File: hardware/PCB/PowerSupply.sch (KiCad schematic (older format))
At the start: 15 parts, among them IC1 BQ24092DGQR, IC4 TPS62291DRVR, J3 S2B-XH-A_LF__SN_

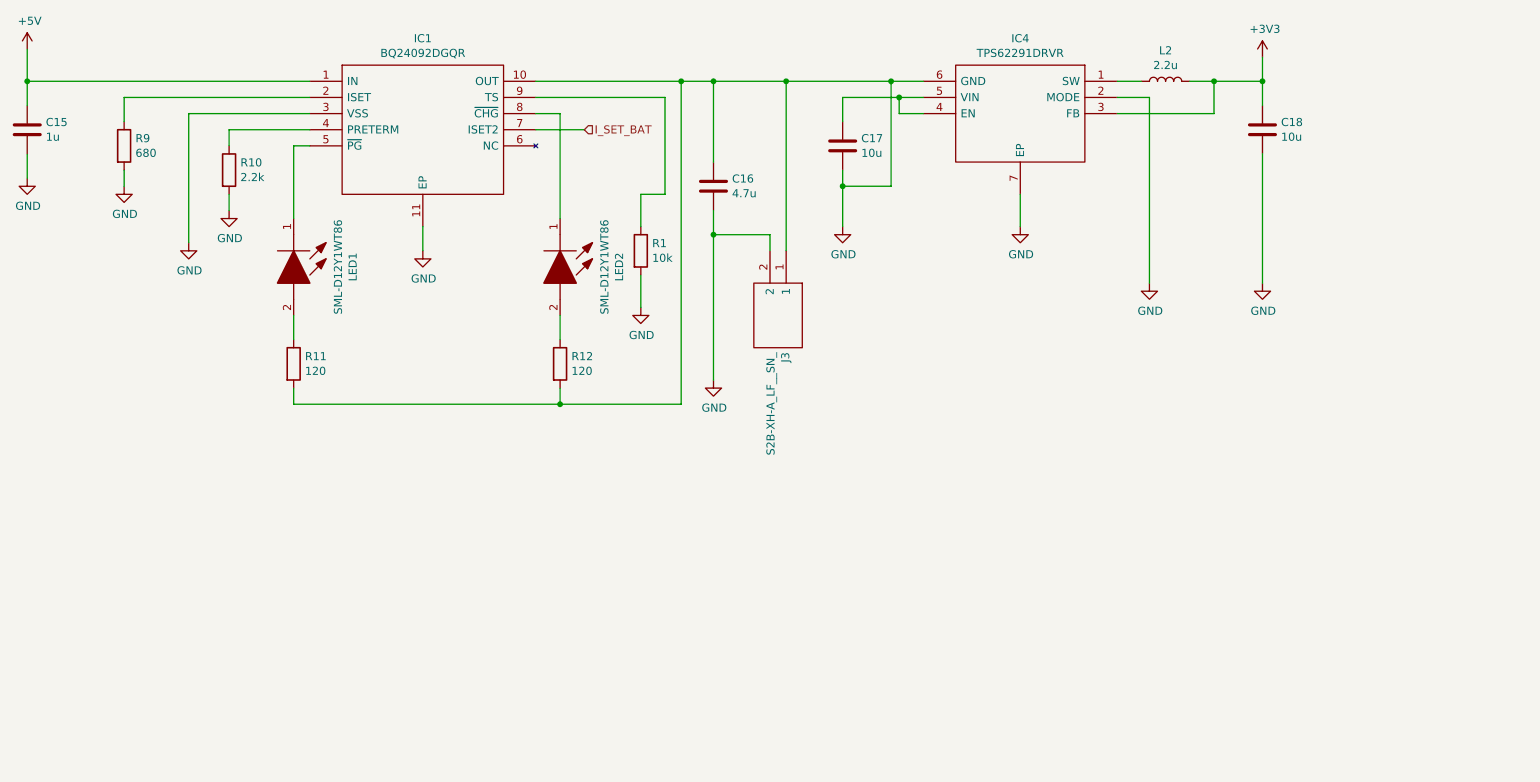
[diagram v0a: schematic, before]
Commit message: add inductor footprint LPS4018
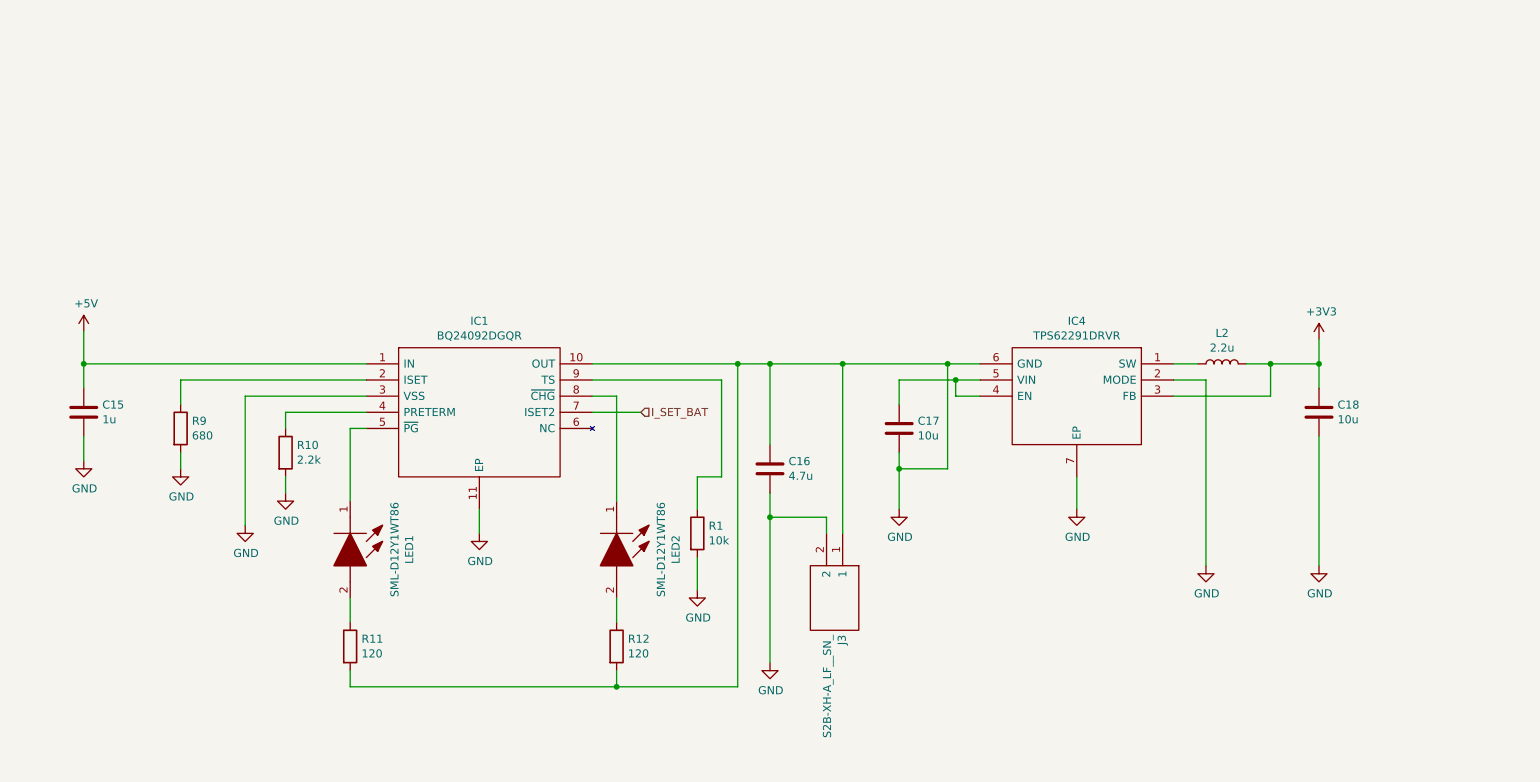
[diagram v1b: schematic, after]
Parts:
- C18: footprint (none) -> Capacitor_SMD:C_0603_1608Metric
- L2: footprint (none) -> Inductor_SMD:L_Coilcraft_LPS4018; Mouser Part Number (none) -> 994-LPS4018-222MRB
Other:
- moved on the sheet: C15, C16, C17, C18, IC1, IC4, J3, L2, LED1, LED2, R1, R10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

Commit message: corrected power supply schematic
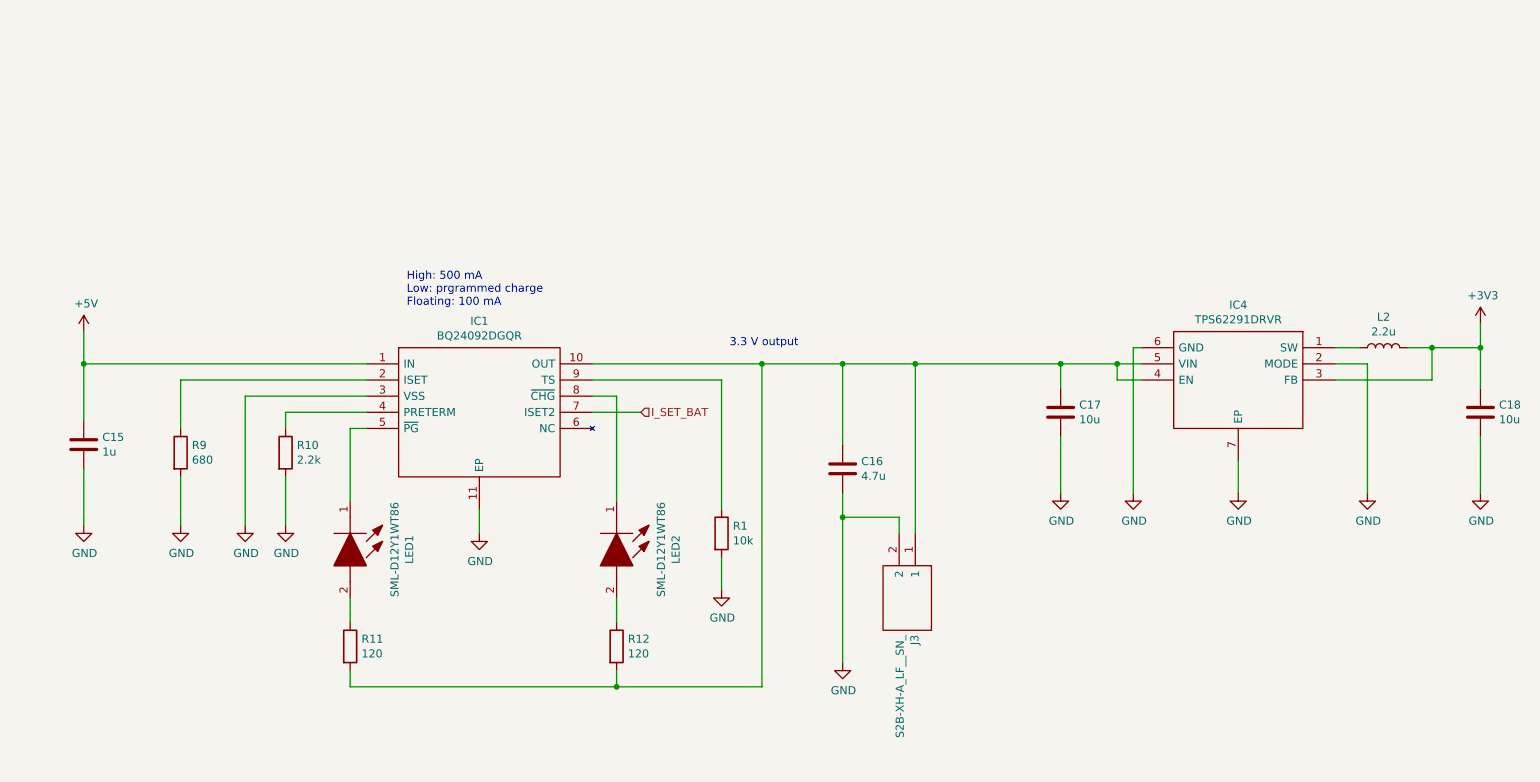
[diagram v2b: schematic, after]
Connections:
- net GND: no longer C16.1, IC1.10 (OUT), J3.1, R11.2, R12.2
- net at C17.1, IC4.4 (EN), IC4.5 (VIN): now also C16.1, IC1.10 (OUT), J3.1, R11.2, R12.2
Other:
- note added: "3.3 V output"
- note added: "High: 500 mA\nLow: prgrammed charge\nFloating: 100 mA"
- moved on the sheet: C15, C16, C17, C18, IC4, J3, L2, R1, R9
